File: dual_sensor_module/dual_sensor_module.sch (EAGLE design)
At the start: 14 parts, among them IC1 MCP602SN, IC2 TC7660DIL8

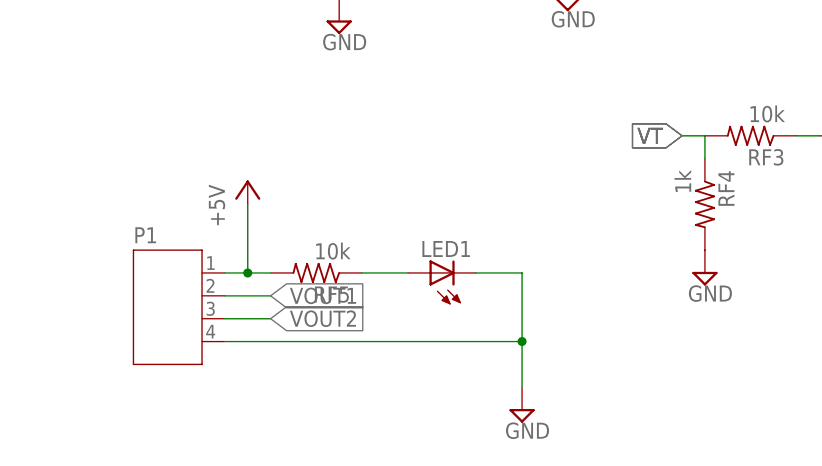
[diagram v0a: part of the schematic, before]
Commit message: agregado plano de tierra y modificadas las imagenes para corte
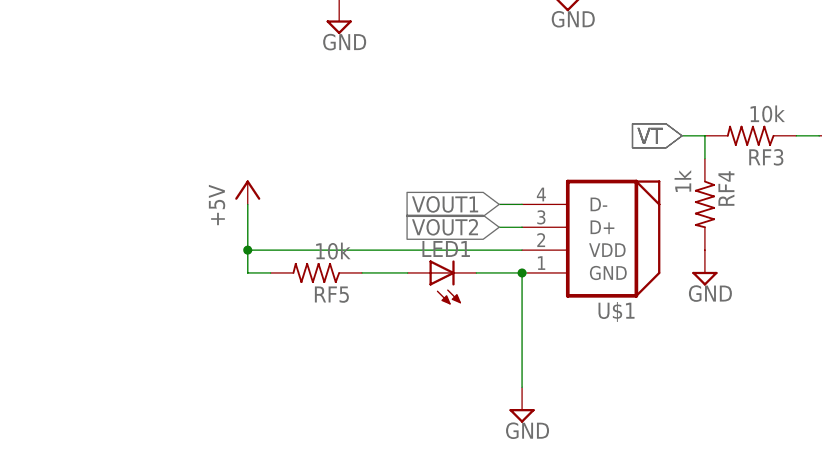
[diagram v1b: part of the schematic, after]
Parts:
- removed P1: (no value), jst-ph:JST-PH4
- added U$1: DYNAMIXEL_RS485, robot-hand:DYNAMIXEL_RS485
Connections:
- net +5V: now also U$1.VDD; no longer P1.1
- net GND: now also U$1.GND; no longer P1.4
- net VOUT1: now also U$1.D-; no longer P1.2
- net VOUT2: now also U$1.D+; no longer P1.3
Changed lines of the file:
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@@
 <part name="SUPPLY2" library="supply2" library_urn="urn:adsk.eagle:library:372" deviceset="GND" device=""/>
 <part name="P+4" library="supply1" library_urn="urn:adsk.eagle:library:371" deviceset="+5V" device=""/>
-<part name="P1" library="jst-ph" deviceset="JST-PH4" device=""/>
 <part name="RF5" library="resistor" library_urn="urn:adsk.eagle:library:348" deviceset="R-US_" device="R0805" package3d_urn="urn:adsk.eagle:package:23553/2" value="10k"/>
 <part name="P+5" library="supply1" library_urn="urn:adsk.eagle:library:371" deviceset="+5V" device=""/>
@@
 <part name="JP1" library="adafruit" deviceset="PINHD-1X3" device=""/>
 <part name="JP2" library="adafruit" deviceset="PINHD-1X3" device=""/>
+<part name="U$1" library="robot-hand" deviceset="DYNAMIXEL_RS485" device=""/>
 </parts>
 <sheets>
@@
 <attribute name="VALUE" x="33.02" y="86.36" size="1.778" layer="96" rot="R90"/>
 </instance>
-<instance part="P1" gate="A" x="15.24" y="30.48" smashed="yes">
-<attribute name="NAME" x="12.7" y="36.322" size="1.778" layer="95"/>
-<attribute name="VALUE" x="12.7" y="20.574" size="1.778" layer="96"/>
-</instance>
 <instance part="RF5" gate="G$1" x="33.02" y="33.02" smashed="yes" rot="R180">
 <attribute name="NAME" x="36.83" y="31.5214" size="1.778" layer="95" rot="R180"/>
@@
 <attribute name="NAME" x="115.57" y="29.845" size="1.778" layer="95" rot="R180"/>
 <attribute name="VALUE" x="115.57" y="43.18" size="1.778" layer="96" rot="R180"/>
+</instance>
+<instance part="U$1" gate="J$1" x="63.5" y="38.1" smashed="yes" rot="R180">
+<attribute name="NAME" x="68.58" y="29.718" size="1.778" layer="95" rot="R180"/>
 </instance>
 </instances>
@@
 <pinref part="SUPPLY3" gate="GND" pin="GND"/>
 <wire x1="50.8" y1="33.02" x2="55.88" y2="33.02" width="0.1524" layer="91"/>
-<wire x1="55.88" y1="33.02" x2="55.88" y2="25.4" width="0.1524" layer="91"/>
-<pinref part="P1" gate="A" pin="4"/>
-<wire x1="55.88" y1="25.4" x2="55.88" y2="20.32" width="0.1524" layer="91"/>
-<wire x1="22.86" y1="25.4" x2="55.88" y2="25.4" width="0.1524" layer="91"/>
-<junction x="55.88" y="25.4"/>
+<wire x1="55.88" y1="33.02" x2="55.88" y2="20.32" width="0.1524" layer="91"/>
+<pinref part="U$1" gate="J$1" pin="GND"/>
+<junction x="55.88" y="33.02"/>
 </segment>
 <segment>
@@
 </segment>
 <segment>
-<pinref part="P1" gate="A" pin="1"/>
 <pinref part="RF5" gate="G$1" pin="2"/>
-<wire x1="22.86" y1="33.02" x2="25.4" y2="33.02" width="0.1524" layer="91"/>
 <pinref part="P+5" gate="1" pin="+5V"/>
 <wire x1="25.4" y1="33.02" x2="27.94" y2="33.02" width="0.1524" layer="91"/>
-<wire x1="25.4" y1="40.64" x2="25.4" y2="33.02" width="0.1524" layer="91"/>
-<junction x="25.4" y="33.02"/>
+<wire x1="25.4" y1="40.64" x2="25.4" y2="35.56" width="0.1524" layer="91"/>
+<pinref part="U$1" gate="J$1" pin="VDD"/>
+<wire x1="25.4" y1="35.56" x2="25.4" y2="33.02" width="0.1524" layer="91"/>
+<wire x1="25.4" y1="35.56" x2="55.88" y2="35.56" width="0.1524" layer="91"/>
+<junction x="25.4" y="35.56"/>
 </segment>
 </net>
@@
 </segment>
 <segment>
-<pinref part="P1" gate="A" pin="2"/>
-<wire x1="22.86" y1="30.48" x2="27.94" y2="30.48" width="0.1524" layer="91"/>
-<label x="27.94" y="30.48" size="1.778" layer="95" xref="yes"/>
+<pinref part="U$1" gate="J$1" pin="D-"/>
+<wire x1="55.88" y1="40.64" x2="53.34" y2="40.64" width="0.1524" layer="91"/>
+<label x="53.34" y="40.64" size="1.778" layer="95" rot="R180" xref="yes"/>
 </segment>
 </net>
@@
 </segment>
 <segment>
-<pinref part="P1" gate="A" pin="3"/>
-<wire x1="22.86" y1="27.94" x2="27.94" y2="27.94" width="0.1524" layer="91"/>
-<label x="27.94" y="27.94" size="1.778" layer="95" xref="yes"/>
-</segment>
-</net>
+<pinref part="U$1" gate="J$1" pin="D+"/>
+<wire x1="55.88" y1="38.1" x2="53.34" y2="38.1" width="0.1524" layer="91"/>
+<label x="53.34" y="38.1" size="1.778" layer="95" rot="R180" xref="yes"/>
+</segment>
+</net>
